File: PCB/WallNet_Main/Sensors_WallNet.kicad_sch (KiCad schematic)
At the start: 20 parts, among them J4 Conn_01x04_Pin, J5 Conn_02x12_Counter_Clockwise, Q1 NMOS, SW2 SW, U2 CPT-9019B-SMT-TR

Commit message: bruh
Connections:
- net P00 renamed Buzzer
- net P01 renamed Button
- net P02 renamed TS_RX
- net P03 renamed TS_TX
- net VDD_nRF renamed VDD_nrf
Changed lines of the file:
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@@
 	(wire
 		(pts
+			(xy 35.56 69.85) (xy 39.37 69.85)
+		)
+		(stroke
+			(width 0)
+			(type default)
+		)
+	)
+	(wire
+		(pts
 			(xy 162.56 44.45) (xy 172.72 44.45)
 		)
@@
 	(wire
 		(pts
-			(xy 38.1 69.85) (xy 39.37 69.85)
+			(xy 45.72 41.91) (xy 49.53 41.91)
 		)
 		(stroke
@@
 		)
 	)
-	(label "VDD_nRF"
-		(at 46.99 96.52 180)
-		(effects
-			(font
-				(size 1.27 1.27)
-			)
-			(justify right bottom)
-		)
-	)
 	(label "P27"
 		(at 107.95 49.53 180)
@@
 		)
 	)
-	(label "P01"
-		(at 38.1 69.85 180)
-		(effects
-			(font
-				(size 1.27 1.27)
-			)
-			(justify right bottom)
-		)
-	)
 	(label "P22"
 		(at 16.51 27.94 180)
@@
 		)
 	)
-	(label "P02"
-		(at 46.99 91.44 180)
-		(effects
-			(font
-				(size 1.27 1.27)
-			)
-			(justify right bottom)
-		)
-	)
-	(label "P00"
-		(at 49.53 41.91 180)
-		(effects
-			(font
-				(size 1.27 1.27)
-			)
-			(justify right bottom)
-		)
-	)
 	(label "P20"
 		(at 107.95 34.29 180)
@@
 		)
 	)
-	(label "P03"
-		(at 46.99 93.98 180)
-		(effects
-			(font
-				(size 1.27 1.27)
-			)
-			(justify right bottom)
-		)
-	)
 	(label "P30"
 		(at 16.51 43.18 180)
@@
 		)
 	)
-	(label "VDD_nRF"
-		(at 39.37 64.77 180)
-		(effects
-			(font
-				(size 1.27 1.27)
-			)
-			(justify right bottom)
-		)
-	)
 	(label "P14"
 		(at 16.51 15.24 180)
@@
 		)
 	)
+	(global_label "VDD_nrf"
+		(shape input)
+		(at 39.37 64.77 180)
+		(fields_autoplaced yes)
+		(effects
+			(font
+				(size 1.27 1.27)
+			)
+			(justify right)
+		)
+		(property "Intersheetrefs" "${INTERSHEET_REFS}"
+			(at 29.1277 64.77 0)
+			(effects
+				(font
+					(size 1.27 1.27)
+				)
+				(justify right)
+				(hide yes)
+			)
+		)
+	)
+	(global_label "VDD_nrf"
+		(shape input)
+		(at 46.99 96.52 180)
+		(fields_autoplaced yes)
+		(effects
+			(font
+				(size 1.27 1.27)
+			)
+			(justify right)
+		)
+		(property "Intersheetrefs" "${INTERSHEET_REFS}"
+			(at 36.7477 96.52 0)
+			(effects
+				(font
+					(size 1.27 1.27)
+				)
+				(justify right)
+				(hide yes)
+			)
+		)
+	)
+	(hierarchical_label "Button"
+		(shape output)
+		(at 35.56 69.85 180)
+		(effects
+			(font
+				(size 1.27 1.27)
+			)
+			(justify right)
+		)
+	)
+	(hierarchical_label "TS_TX"
+		(shape bidirectional)
+		(at 46.99 93.98 180)
+		(effects
+			(font
+				(size 1.27 1.27)
+			)
+			(justify right)
+		)
+	)
+	(hierarchical_label "TS_RX"
+		(shape bidirectional)
+		(at 46.99 91.44 180)
+		(effects
+			(font
+				(size 1.27 1.27)
+			)
+			(justify right)
+		)
+	)
+	(hierarchical_label "Buzzer"
+		(shape output)
+		(at 45.72 41.91 180)
+		(effects
+			(font
+				(size 1.27 1.27)
+			)
+			(justify right)
+		)
+	)

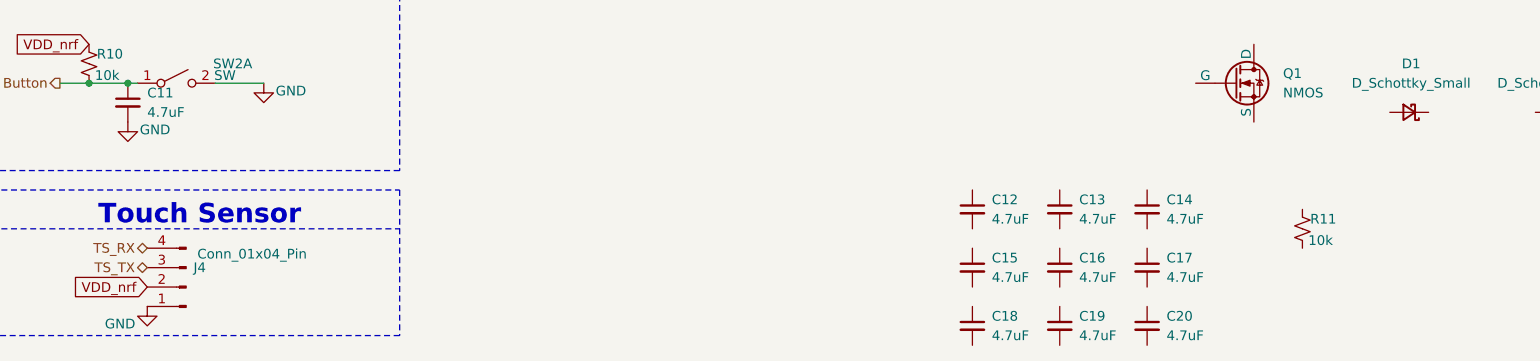
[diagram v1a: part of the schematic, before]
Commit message: Changed some Heir connections
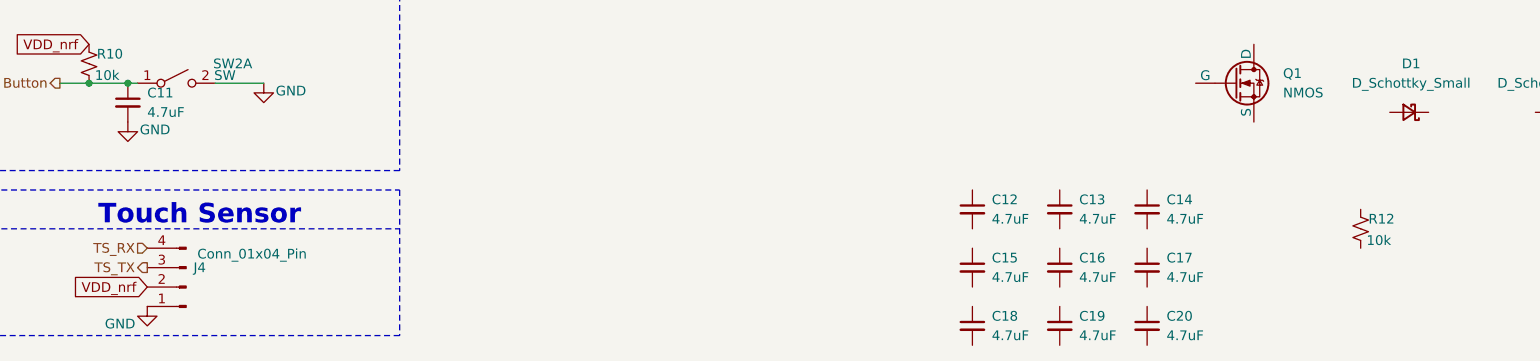
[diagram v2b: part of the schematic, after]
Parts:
- removed R11: 10k, symbol Device:R_Small_US
- added R12: 10k, symbol Device:R_Small_US
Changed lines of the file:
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@@
 	)
 	(hierarchical_label "TS_TX"
-		(shape bidirectional)
+		(shape output)
 		(at 46.99 93.98 180)
 		(effects
@@
 	)
 	(hierarchical_label "TS_RX"
-		(shape bidirectional)
+		(shape input)
 		(at 46.99 91.44 180)
 		(effects
@@
 	)
 	(symbol
-		(lib_id "Device:R_Small_US")
-		(at 198.12 88.9 0)
-		(unit 1)
-		(exclude_from_sim no)
-		(in_bom yes)
-		(on_board yes)
-		(dnp no)
-		(property "Reference" "R11"
-			(at 199.136 87.63 0)
-			(effects
-				(font
-					(size 1.27 1.27)
-				)
-				(justify left)
-			)
-		)
-		(property "Value" "10k"
-			(at 198.882 90.424 0)
-			(effects
-				(font
-					(size 1.27 1.27)
-				)
-				(justify left)
-			)
-		)
-		(property "Footprint" ""
-			(at 198.12 88.9 0)
-			(effects
-				(font
-					(size 1.27 1.27)
-				)
-				(hide yes)
-			)
-		)
-		(property "Datasheet" "~"
-			(at 198.12 88.9 0)
-			(effects
-				(font
-					(size 1.27 1.27)
-				)
-				(hide yes)
-			)
-		)
-		(property "Description" "Resistor, small US symbol"
-			(at 198.12 88.9 0)
-			(effects
-				(font
-					(size 1.27 1.27)
-				)
-				(hide yes)
-			)
-		)
-		(pin "1"
-		)
-		(pin "2"
-		)
-		(instances
-			(project "WallNet_Main"
-				(path "/3272dd14-9e34-4275-b10b-c06dab1b3ca1/14f35c0a-7540-4617-95f9-116bbddd487f"
-					(reference "R11")
-					(unit 1)
-				)
-			)
-		)
-	)
-	(symbol
 		(lib_id "Device:C_Small")
 		(at 154.94 101.6 0)
@@
 					(unit 1)
 				)
+			)
+		)
+	)
+	(symbol
+		(lib_id "Device:R_Small_US")
+		(at 205.74 88.9 0)
+		(unit 1)
+		(exclude_from_sim no)
+		(in_bom yes)
+		(on_board yes)
+		(dnp no)
+		(property "Reference" "R12"
+			(at 206.756 87.63 0)
+			(effects
+				(font
+					(size 1.27 1.27)
+				)
+				(justify left)
+			)
+		)
+		(property "Value" "10k"
+			(at 206.502 90.424 0)
+			(effects
+				(font
+					(size 1.27 1.27)
+				)
+				(justify left)
+			)
+		)
+		(property "Footprint" ""
+			(at 205.74 88.9 0)
+			(effects
+				(font
+					(size 1.27 1.27)
+				)
+				(hide yes)
+			)
+		)
+		(property "Datasheet" "~"
+			(at 205.74 88.9 0)
+			(effects
+				(font
+					(size 1.27 1.27)
+				)
+				(hide yes)
+			)
+		)
+		(property "Description" "Resistor, small US symbol"
+			(at 205.74 88.9 0)
+			(effects
+				(font
+					(size 1.27 1.27)
+				)
+				(hide yes)
+			)
+		)
+		(pin "1"
+		)
+		(pin "2"
+		)
+		(instances
+			(project "WallNet_Main"
+				(path "/3272dd14-9e34-4275-b10b-c06dab1b3ca1/14f35c0a-7540-4617-95f9-116bbddd487f"
+					(reference "R12")
+					(unit 1)
+				)

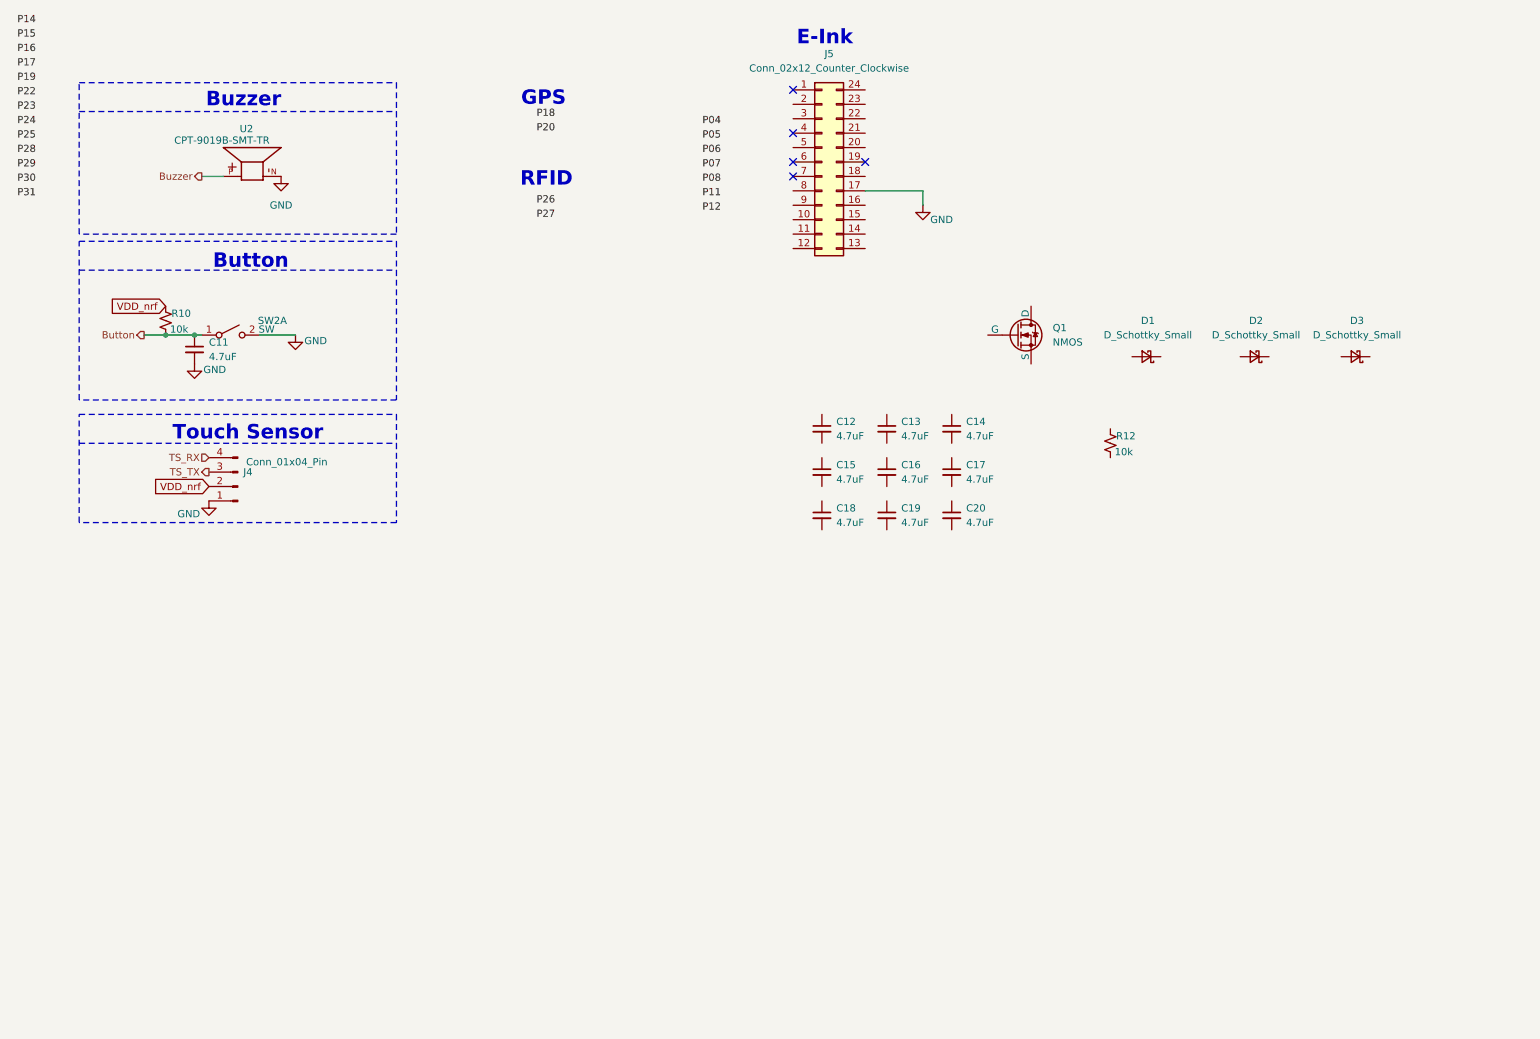
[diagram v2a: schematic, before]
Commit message: E-ink & GPS connection Complete
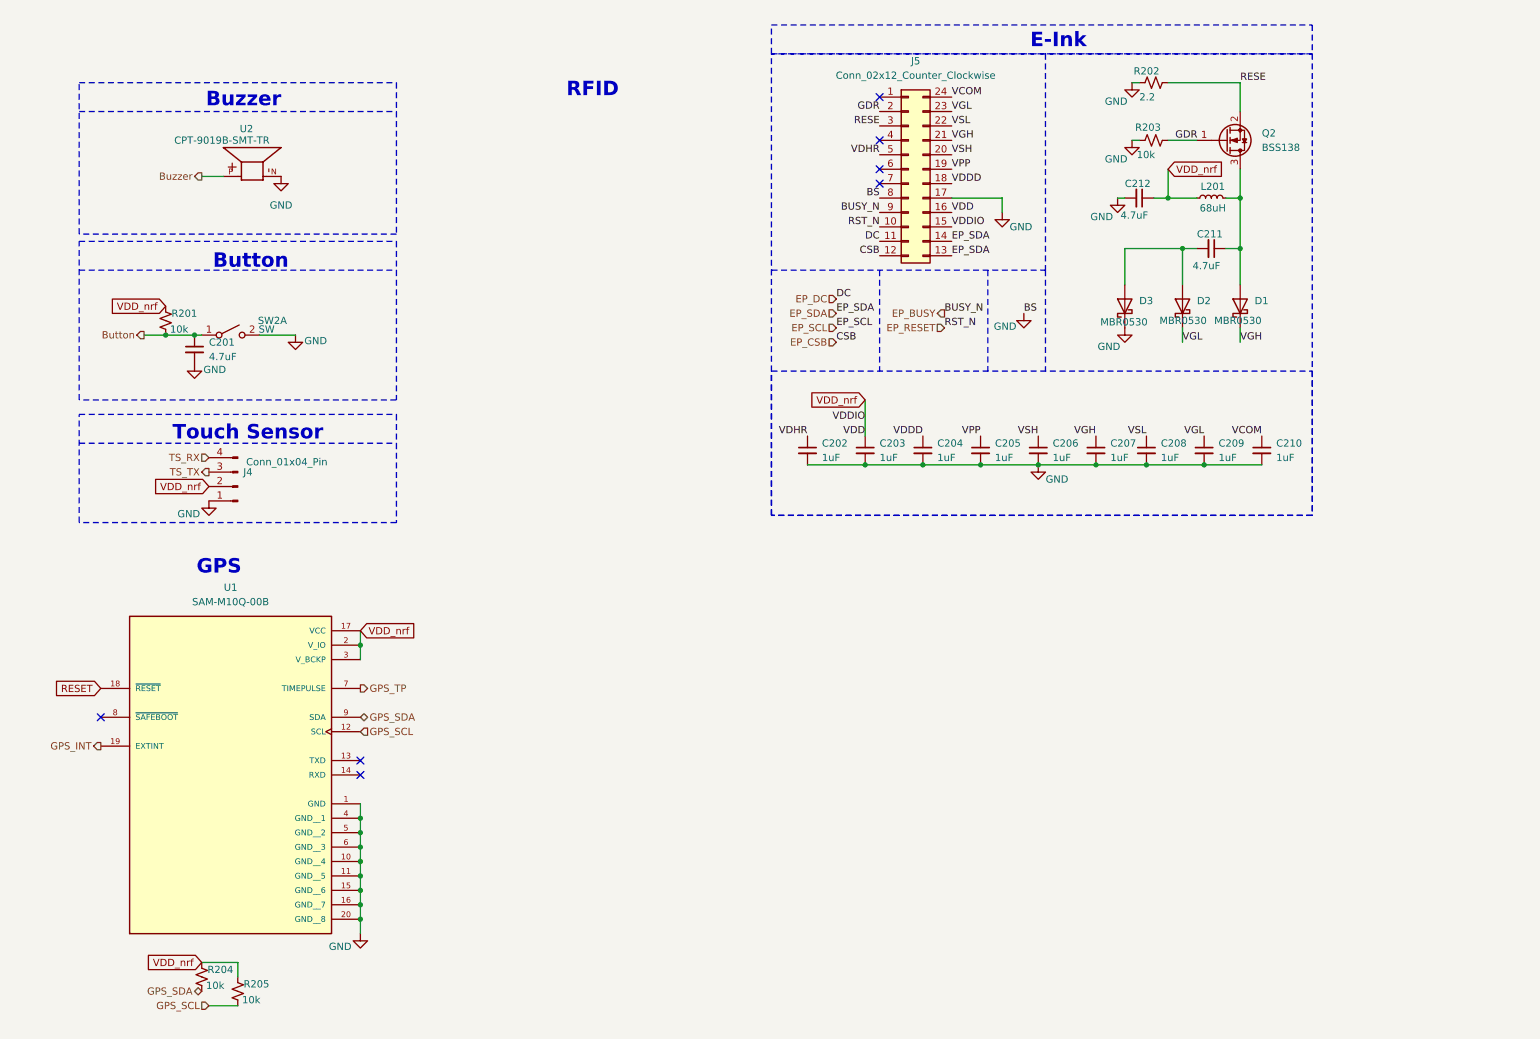
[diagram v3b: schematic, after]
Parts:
- removed D1, D2, D3: D_Schottky_Small, symbol Device:D_Schottky_Small
- removed Q1: NMOS, symbol Simulation_SPICE:NMOS
- added C211, C212: 4.7uF, symbol Device:C_Small
- added D1, D2, D3: MBR0530, Diode_SMD:D_SOD-123, symbol Diode:MBR0530
- added L201: 68uH, symbol Device:L_Small
- added Q2: BSS138, Package_TO_SOT_SMD:SOT-23, symbol Transistor_FET:BSS138
- added R203, R204, R205: 10k, symbol Device:R_Small_US
- added U1: SAM-M10Q-00B, SAM-M10Q-00B:XCVR_SAM-M10Q-00B, symbol SAM-M10Q-00B:SAM-M10Q-00B
- C202: renamed from C13; value 4.7uF -> 1uF
- C203: renamed from C14; value 4.7uF -> 1uF
- C204: renamed from C15; value 4.7uF -> 1uF
- C205: renamed from C16; value 4.7uF -> 1uF
- C206: renamed from C17; value 4.7uF -> 1uF
- C207: renamed from C18; value 4.7uF -> 1uF
- C208: renamed from C19; value 4.7uF -> 1uF
- C209: renamed from C20; value 4.7uF -> 1uF
- C210: renamed from C12; value 4.7uF -> 1uF
- R202: renamed from R12; value 10k -> 2.2
- renumbered C11 to C201, R10 to R201
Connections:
- net GND: now also C202.2, C203.2, C204.2, C205.2, C206.2, C207.2, C208.2, C209.2, C210.2, J5.8 (Pin_8), R202.1, C212.2, D3.1 (K), R203.1, U1.1 (GND), U1.10 (GND__4), U1.11 (GND__5), U1.15 (GND__6), U1.16 (GND__7), U1.20 (GND__8), U1.4 (GND__1), U1.5 (GND__2), U1.6 (GND__3)
- net VDD_nrf: now also C203.1, J5.15 (Pin_15), J5.16 (Pin_16), C212.1, L201.1, R204.1, R205.1, U1.17 (VCC), U1.2 (V_IO), U1.3 (V_BCKP)
- net VGH: now reaches C207.1
- net VGH: now also J5.21 (Pin_21), D1.1 (K)
- net VDHR: now reaches C202.1
- net VDHR: now also J5.5 (Pin_5)
- net VSH: now reaches C206.1
- net VSH: now also J5.20 (Pin_20)
- net VSL: now reaches C208.1
- net VSL: now also J5.22 (Pin_22)
- net VCOM: now reaches C210.1
- net VCOM: now also J5.24 (Pin_24)
- net EP_RESET: now reaches J5.10 (Pin_10)
- net EP_DC: now reaches J5.11 (Pin_11)
- net EP_CSB: now reaches J5.12 (Pin_12)
- net EP_SDA: now reaches J5.13 (Pin_13)
- net EP_SDA: now also J5.14 (Pin_14)
- net VDDD: now reaches J5.18 (Pin_18)
- net VDDD: now also C204.1
- net VPP: now reaches J5.19 (Pin_19)
- net VPP: now also C205.1
- net GDR: now reaches J5.2 (Pin_2)
- net GDR: now also Q2.1 (G), R203.2
- net VGL: now reaches J5.23 (Pin_23)
- net VGL: now also C209.1, D2.1 (K)
- net RESE: now reaches J5.3 (Pin_3)
- net RESE: now also R202.2, Q2.2 (S)
- net EP_BUSY: now reaches J5.9 (Pin_9)
- new net: C211.1, D1.2 (A), L201.2, Q2.3 (D)
- new net: C211.2, D2.2 (A), D3.2 (A)
- new net GPS_INT: U1.19 (EXTINT)
- new net GPS_SCL: R205.2, U1.12 (SCL)
- new net GPS_SDA: R204.2, U1.9 (SDA)
- new net GPS_TP: U1.7 (TIMEPULSE)
- new net RESET: U1.18 (~{RESET})
- no-connect marks 5 -> 7
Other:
- moved on the sheet: C202, C203, C204, C205, C206, C207, C208, C209, C210, J5, R202

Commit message: Parts complete for schematic
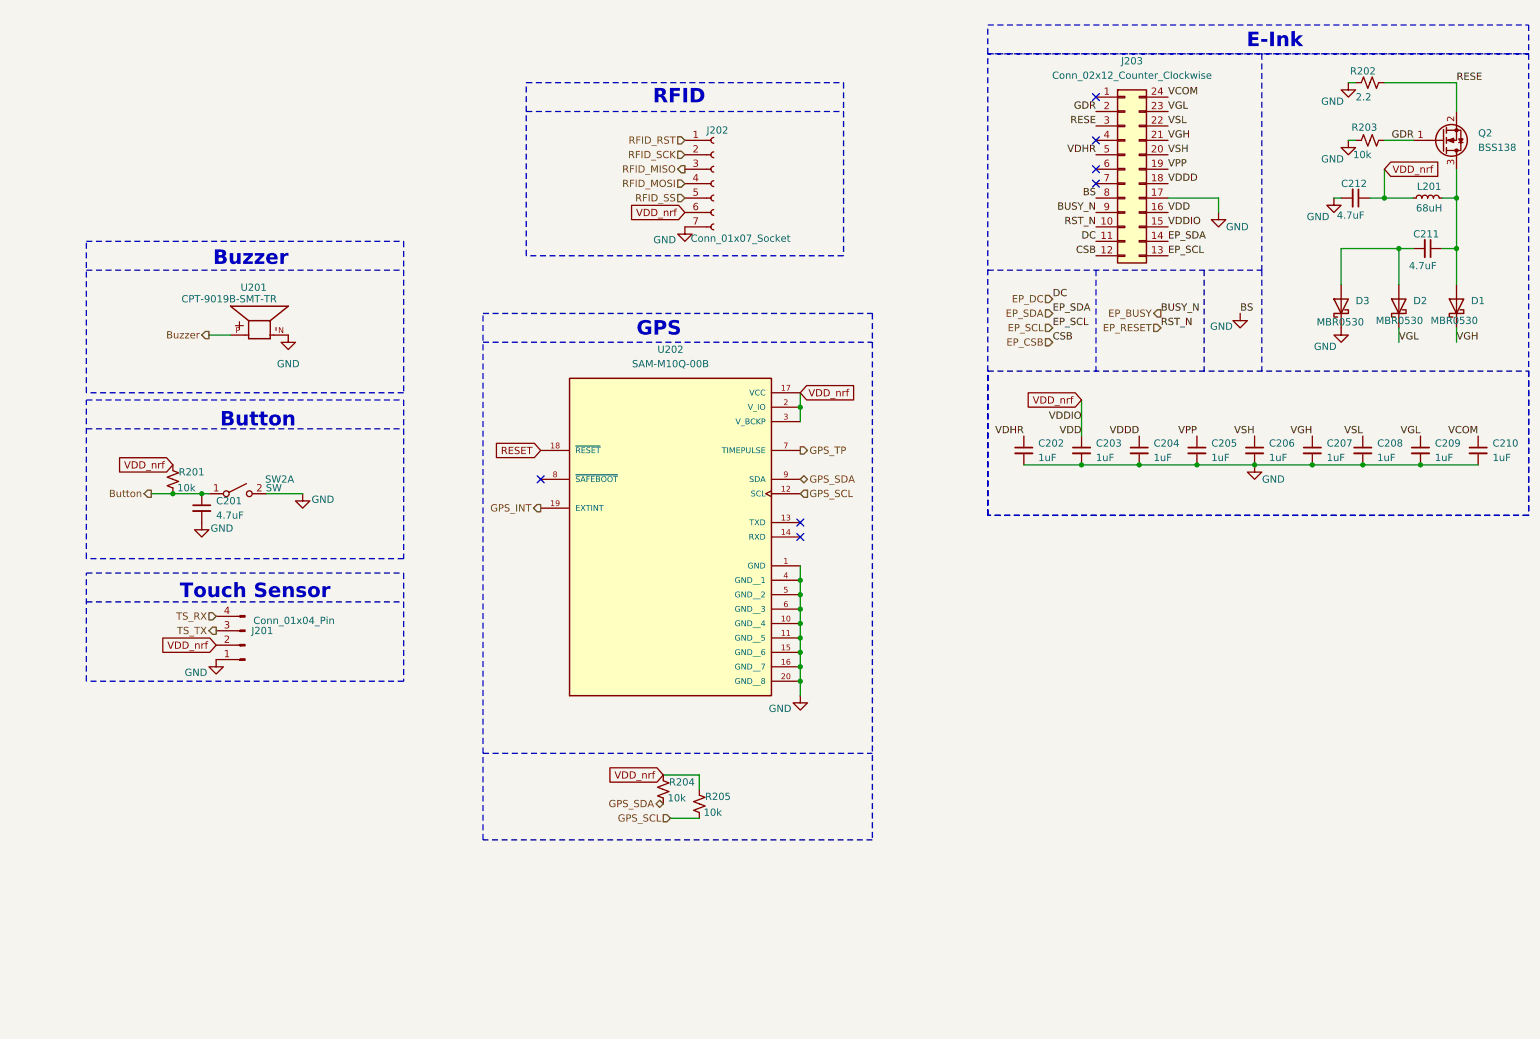
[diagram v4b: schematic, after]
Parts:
- added J202: Conn_01x07_Socket, Connector_PinSocket_2.00mm:PinSocket_1x07_P2.00mm_Horizontal, symbol Connector:Conn_01x07_Socket
- C201, C202, C203, C204, C205, C206, C207, C208, C209, C210, C211, C212: footprint (none) -> Capacitor_SMD:C_0201_0603Metric
- R201, R202, R203, R204, R205: footprint (none) -> Resistor_SMD:R_0201_0603Metric
- U202: renamed from U1; footprint SAM-M10Q-00B:XCVR_SAM-M10Q-00B -> SAM_M10Q_00B:XCVR_SAM-M10Q-00B
- renumbered J4 to J201, J5 to J203, U2 to U201
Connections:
- net EP_SCL: now also J203.13 (Pin_13)
- net EP_SDA: no longer J203.13 (Pin_13)
- net GND: now also J202.7 (Pin_7)
- net VDD_nrf: now also J202.6 (Pin_6)
- new net RFID_MISO: J202.3 (Pin_3)
- new net RFID_MOSI: J202.4 (Pin_4)
- new net RFID_RST: J202.1 (Pin_1)
- new net RFID_SCK: J202.2 (Pin_2)
- new net RFID_SS: J202.5 (Pin_5)
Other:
- moved on the sheet: C201, C202, C203, C204, C205, C206, C207, C208, C209, C210, C211, C212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
